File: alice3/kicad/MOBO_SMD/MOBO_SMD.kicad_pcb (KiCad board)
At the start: 2 copper layers, 90.4 x 49 mm, 53 parts, among them CON1 MicroSD, P1 CONN_01X05, P2 USB_OTG, P3 UART1, SW1 RESET, SW2 SOFT RESET, U1 VGA_daughter_board, U2 Propeller_P8X32A-D40, U3 24LC256, U4 Propeller_Plug, U5 STM32F415RG, U6 Z80CPU, U7 71V424S15PHGI8, U8 LD29080DT33R, Y1 5 MHz, Y2 16MHz, Y3 32.768KHz

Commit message: First pass at board layout.
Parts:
- removed C12, C13: 22pF, Capacitors_SMD:C_0805
- removed C18: 0.1 µF, Capacitors_SMD:C_0805
- removed R13, R5: 10k, Resistors_SMD:R_0805
- removed U7: 71V424S15PHGI8, TSOP44-II:TSOP44-II
- removed Y3: 32.768KHz, Crystals:Crystal_HC50-U_Vertical
- added C21: 1µ, Capacitors_SMD:C_0805, F.Cu at (180.5, 170.6)
- added C22: 4.7µ, Capacitors_SMD:C_1206, F.Cu at (171.0, 172.0)
- added F1: F_Small, Resistors_SMD:R_1210, F.Cu at (194.3, 83.8)
- added J1: VGA, Jac:00JG-DB15HDSOCKET, F.Cu at (165.1, 86.4)
- added R14: 240, Resistors_SMD:R_0805, F.Cu at (187.0, 134.0)
- added R15: 470, Resistors_SMD:R_0805, F.Cu at (187.0, 140.3)
- added R16: 240, Resistors_SMD:R_0805, F.Cu at (190.6, 134.0)
- added R17: 470, Resistors_SMD:R_0805, F.Cu at (204.5, 102.9)
- added R18: 240, Resistors_SMD:R_0805, F.Cu at (194.3, 134.0)
- added R19: 470, Resistors_SMD:R_0805, F.Cu at (190.6, 140.3)
- added R20: 240, Resistors_SMD:R_0805, F.Cu at (203.2, 127.0)
- added R21: 240, Resistors_SMD:R_0805, F.Cu at (194.3, 140.3)
- added R22: 10K, Resistors_SMD:R_0805, F.Cu at (176.7, 170.6)
- added R23: 10K, Resistors_SMD:R_0805, F.Cu at (201.9, 95.2)
- added R24: 100, Resistors_SMD:R_0805, F.Cu at (170.3, 178.5)
- added R25: 100, Resistors_SMD:R_0805, F.Cu at (176.7, 164.3)
- added REF**: 1pin, Connect:1pin, F.Cu at (113.0, 77.5)
- added REF**: 1pin, Connect:1pin, F.Cu at (113.0, 118.1)
- added REF**: 1pin, Connect:1pin, F.Cu at (195.6, 118.1)
- added REF**: 1pin, Connect:1pin, F.Cu at (195.6, 77.5)
- added X1: MINI_DIN_6, cui-md-xxs:cui-md-60s, F.Cu at (141.0, 74.9)
- C14, C19, C20: footprint Capacitors_ThroughHole:C_Radial_D5_L11_P2.5 -> Capacitors_SMD:C_1206
- D1: value DEBUG -> DEBUG LED; footprint LEDs:LED_0805 -> LEDs:LED-0805
- R1: value 100 -> 10k
- R11: value 1k -> 10k
- R12: value 1k -> 100
- SW1, SW2: footprint Buttons_Switches_ThroughHole:SW_PUSH_SMALL -> Buttons_Switches_SMD:SW_SPST_PTS645
- U1: value VGA_daughter_board -> Z80CPU-SMD; footprint Pin_Headers:Pin_Header_Straight_1x14 -> Housings_QFP:LQFP-44_10x10mm_Pitch0.8mm
- U2: value Propeller_P8X32A-D40 -> Propeller_P8X32A-Q44
- U6: value Z80CPU -> AS6C2008_TSOP; footprint Housings_QFP:LQFP-44_10x10mm_Pitch0.8mm -> SMD_Packages:TSOP32SP
- Y1: footprint Crystals:Crystal_HC50-U_Vertical -> Crystals:Crystal_HC49-SD_SMD
- Y2: footprint Crystals:Crystal_HC50-U_Vertical -> Crystals:ABM3
- moved Y2 58.8 mm to (113.0, 101.6), turned to 90 degrees
- moved C15 57.6 mm to (193.0, 92.7)
- moved U1 54.7 mm to (144.8, 101.6)
- moved C8 54.0 mm to (146.1, 132.1)
- moved Y1 53.7 mm to (224.8, 92.7)
- moved C11 51.5 mm to (138.4, 138.4)
- moved C4 44.4 mm to (131.3, 136.7)
- moved D1 41.1 mm to (141.0, 115.6), turned to 90 degrees
- moved U8 40.2 mm to (186.7, 86.4)
- moved D2 39.7 mm to (144.8, 115.6), turned to 90 degrees
- moved R2 38.8 mm to (213.4, 118.1)
- moved C3 37.5 mm to (152.7, 137.7)
- moved C5 37.5 mm to (152.9, 147.1)
- moved C6 37.5 mm to (144.0, 143.3)
- moved R10 37.5 mm to (148.1, 143.3)
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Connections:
- D1 pad 1: Net-(D1-Pad1) -> GND
- JP1 pad 1: Net-(JP1-Pad1) -> +3V3
- JP1 pad 2: GND -> Net-(JP1-Pad2)
- P2 pad 1: +5V -> Net-(F1-Pad1)
- P2 pad S4: (no net) -> GND
- R1 pad 1: Net-(D1-Pad1) -> Net-(R1-Pad1)
- R12 pad 1: +3V3 -> Net-(R1-Pad1)
- R12 pad 2: /BUSRQ -> Net-(D1-Pad2)
- R3 pad 1: +3V3 -> Net-(JP1-Pad2)
- R3 pad 2: Net-(JP1-Pad1) -> GND
- U1 pad 1: Net-(U1-Pad1) -> CLK
- U1 pad 10: Net-(U1-Pad10) -> D1
- U1 pad 11: KBD_DATA -> Net-(U1-Pad11)
- U1 pad 12: KBD_CLK -> +3V3
- U1 pad 13: +5V -> +3V3
- U1 pad 14: GND -> /HALT
- U1 pad 2: Net-(U1-Pad2) -> D4
- U1 pad 3: Net-(U1-Pad3) -> D3
- U1 pad 4: Net-(U1-Pad4) -> D5
- U1 pad 5: Net-(U1-Pad5) -> D6
- U1 pad 6: Net-(U1-Pad6) -> +3V3
- U1 pad 7: Net-(U1-Pad7) -> D2
- U1 pad 8: Net-(U1-Pad8) -> D7
- U1 pad 9: Net-(U1-Pad9) -> D0
- U2 pad 1: Net-(D1-Pad2) -> A7
- U2 pad 10: GND -> VGA_HSYNC
- U2 pad 11: /RESET -> VGA_B0
- U2 pad 12: +3V3 -> VGA_B1
- U2 pad 13: Net-(U1-Pad1) -> VGA_G0
- U2 pad 14: Net-(U1-Pad2) -> VGA_G1
- U2 pad 15: Net-(U1-Pad3) -> VGA_R1
- U2 pad 16: Net-(U1-Pad4) -> VGA_R0
- U2 pad 17: Net-(U1-Pad5) -> GND
- U2 pad 18: Net-(U1-Pad6) -> +3V3
- U2 pad 19: Net-(U1-Pad7) -> D0
- U2 pad 2: /IORQ -> CLK
- U2 pad 20: Net-(U1-Pad8) -> D1
- U2 pad 21: D0 -> D2
- U2 pad 22: D1 -> D3
- U2 pad 23: D2 -> D4
- U2 pad 24: D3 -> D5
- U2 pad 25: D4 -> D6
- U2 pad 26: D5 -> D7
- U2 pad 27: D6 -> GND
- U2 pad 28: D7 -> Net-(U2-Pad28)
- U2 pad 29: GND -> Net-(U2-Pad29)
- U2 pad 3: /WR -> Net-(P1-Pad5)
- U2 pad 30: Net-(U2-Pad30) -> +3V3
- U2 pad 31: Net-(U2-Pad31) -> A0
- U2 pad 32: +3V3 -> A1
- U2 pad 33: A0 -> A2
- U2 pad 34: A1 -> Net-(P1-Pad3)
- U2 pad 35: A2 -> Net-(U2-Pad35)
- U2 pad 36: Net-(P1-Pad3) -> Net-(R2-Pad2)
- U2 pad 38: Net-(R2-Pad2) -> Net-(U2-Pad38)
- U2 pad 39: Net-(U2-Pad39) -> GND
- U2 pad 4: /RD -> Net-(P1-Pad4)
- U2 pad 40: Net-(U2-Pad40) -> +3V3
- U2 pad 41: (no net) -> ~PROP_READY~
- U2 pad 42: (no net) -> /IORQ
- U2 pad 43: (no net) -> /WR
- U2 pad 44: (no net) -> /RD
- U2 pad 5: A7 -> GND
- U2 pad 6: CLK -> GND
- U2 pad 7: Net-(P1-Pad5) -> /RESET
- U2 pad 8: Net-(P1-Pad4) -> +3V3
- U2 pad 9: GND -> VGA_VSYNC
- U3 pad 6: Net-(U2-Pad37) -> Net-(U2-Pad35)
- U4 pad 3: Net-(U2-Pad40) -> Net-(U2-Pad38)
- U4 pad 4: Net-(U2-Pad39) -> Net-(U2-Pad37)
- U5 pad 28: GND -> Net-(R1-Pad1)
- U5 pad 3: Net-(C12-Pad1) -> ~PROP_READY~
- U5 pad 4: Net-(C13-Pad2) -> A17
- U5 pad 60: Net-(JP1-Pad1) -> Net-(JP1-Pad2)
- U6 pad 10: D6 -> A16
- U6 pad 11: +3V3 -> A14
- U6 pad 12: D2 -> A12
- U6 pad 13: D7 -> A7
- U6 pad 14: D0 -> A6
- U6 pad 15: D1 -> A5
- U6 pad 16: +3V3 -> A4
- U6 pad 17: +3V3 -> A3
- U6 pad 18: /HALT -> A2
- U6 pad 19: /MREQ -> A1
- U6 pad 2: A12 -> A9
- U6 pad 20: /IORQ -> A0
- U6 pad 21: /RD -> D0
- U6 pad 22: /WR -> D1
- U6 pad 23: /BUSACK -> D2
- U6 pad 24: +3V3 -> GND
- U6 pad 25: /BUSRQ -> D3
- U6 pad 26: /Z80_RESET -> D4
- U6 pad 27: Net-(U6-Pad27) -> D5
- U6 pad 28: Net-(U6-Pad28) -> D6
- U6 pad 29: GND -> D7
- U6 pad 3: A13 -> A8
- U6 pad 30: A0 -> /MREQ
- U6 pad 31: A1 -> A10
- U6 pad 32: A2 -> /RD
- U6 pad 4: A14 -> A13
- U6 pad 5: A15 -> /WR
- U6 pad 6: CLK -> GND
- U6 pad 7: D4 -> A15
- U6 pad 8: D3 -> +3V3
- U6 pad 9: D5 -> A17
- Y1 pad 1: Net-(U2-Pad30) -> Net-(U2-Pad28)
- Y1 pad 2: Net-(U2-Pad31) -> Net-(U2-Pad29)
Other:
- board size 90.4 x 49 mm -> 90.2 x 48.3 mm

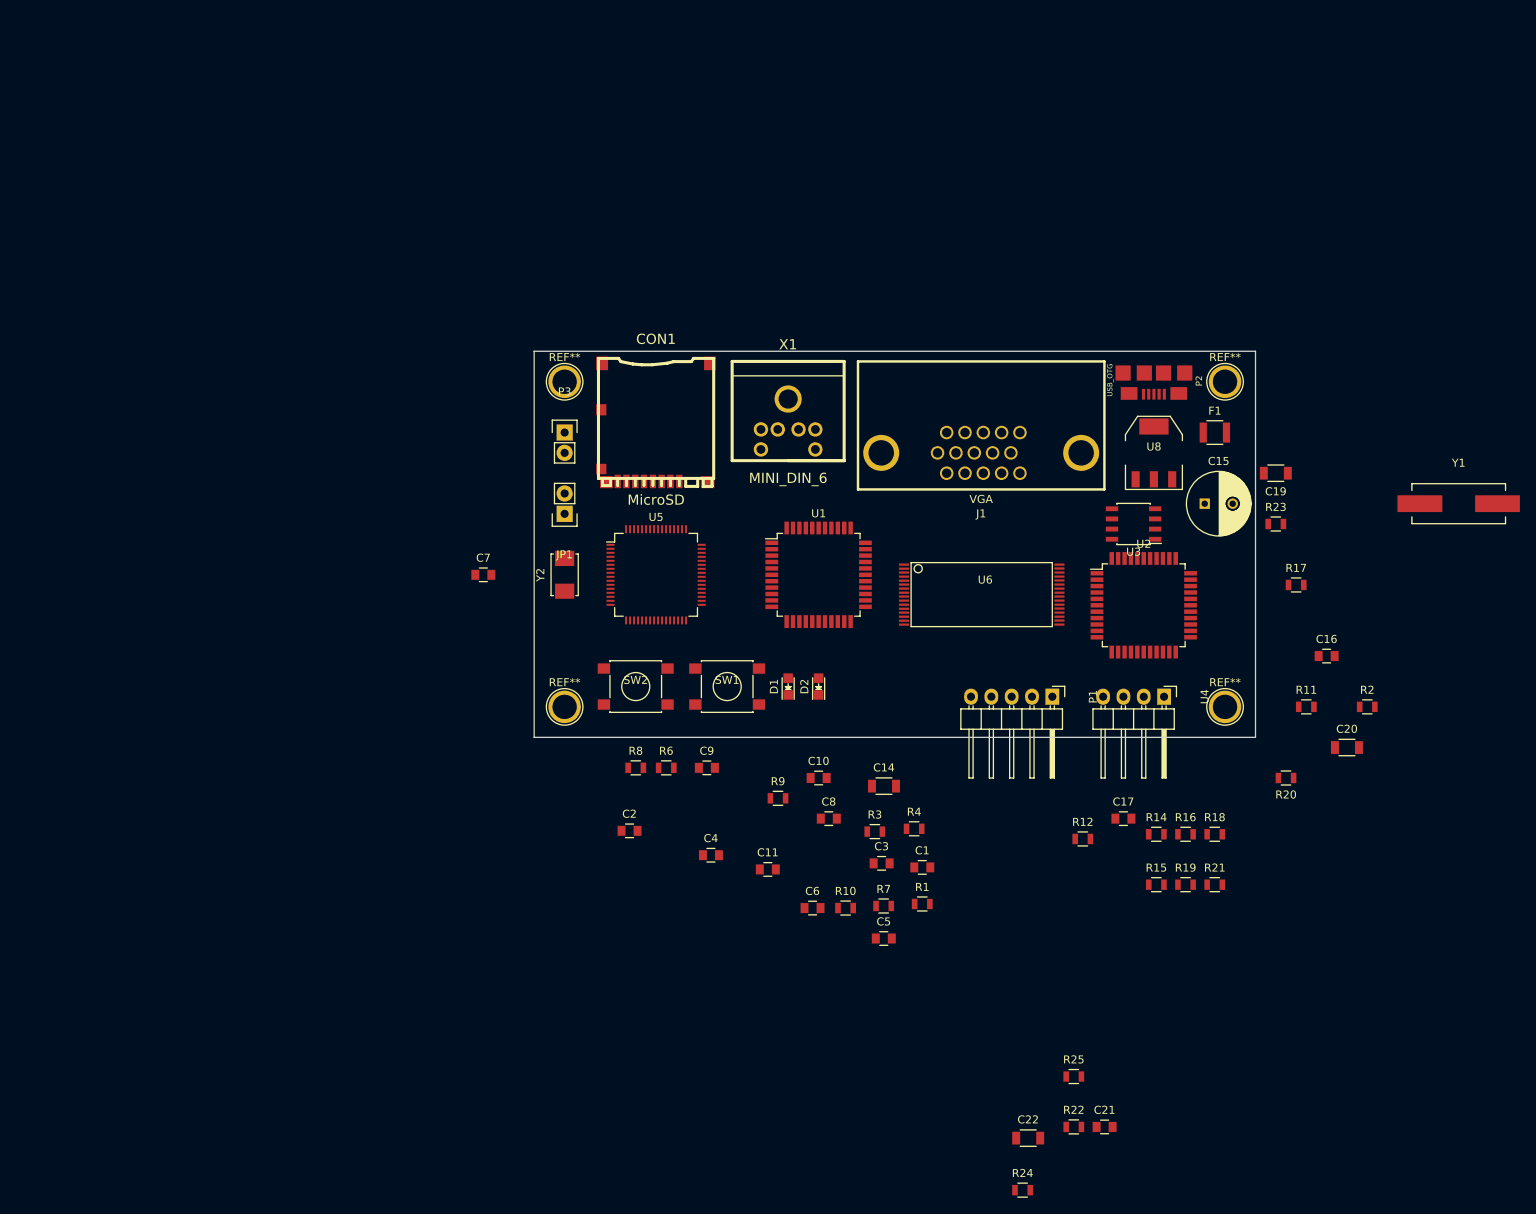
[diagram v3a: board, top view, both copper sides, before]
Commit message: Position all parts on PCB.
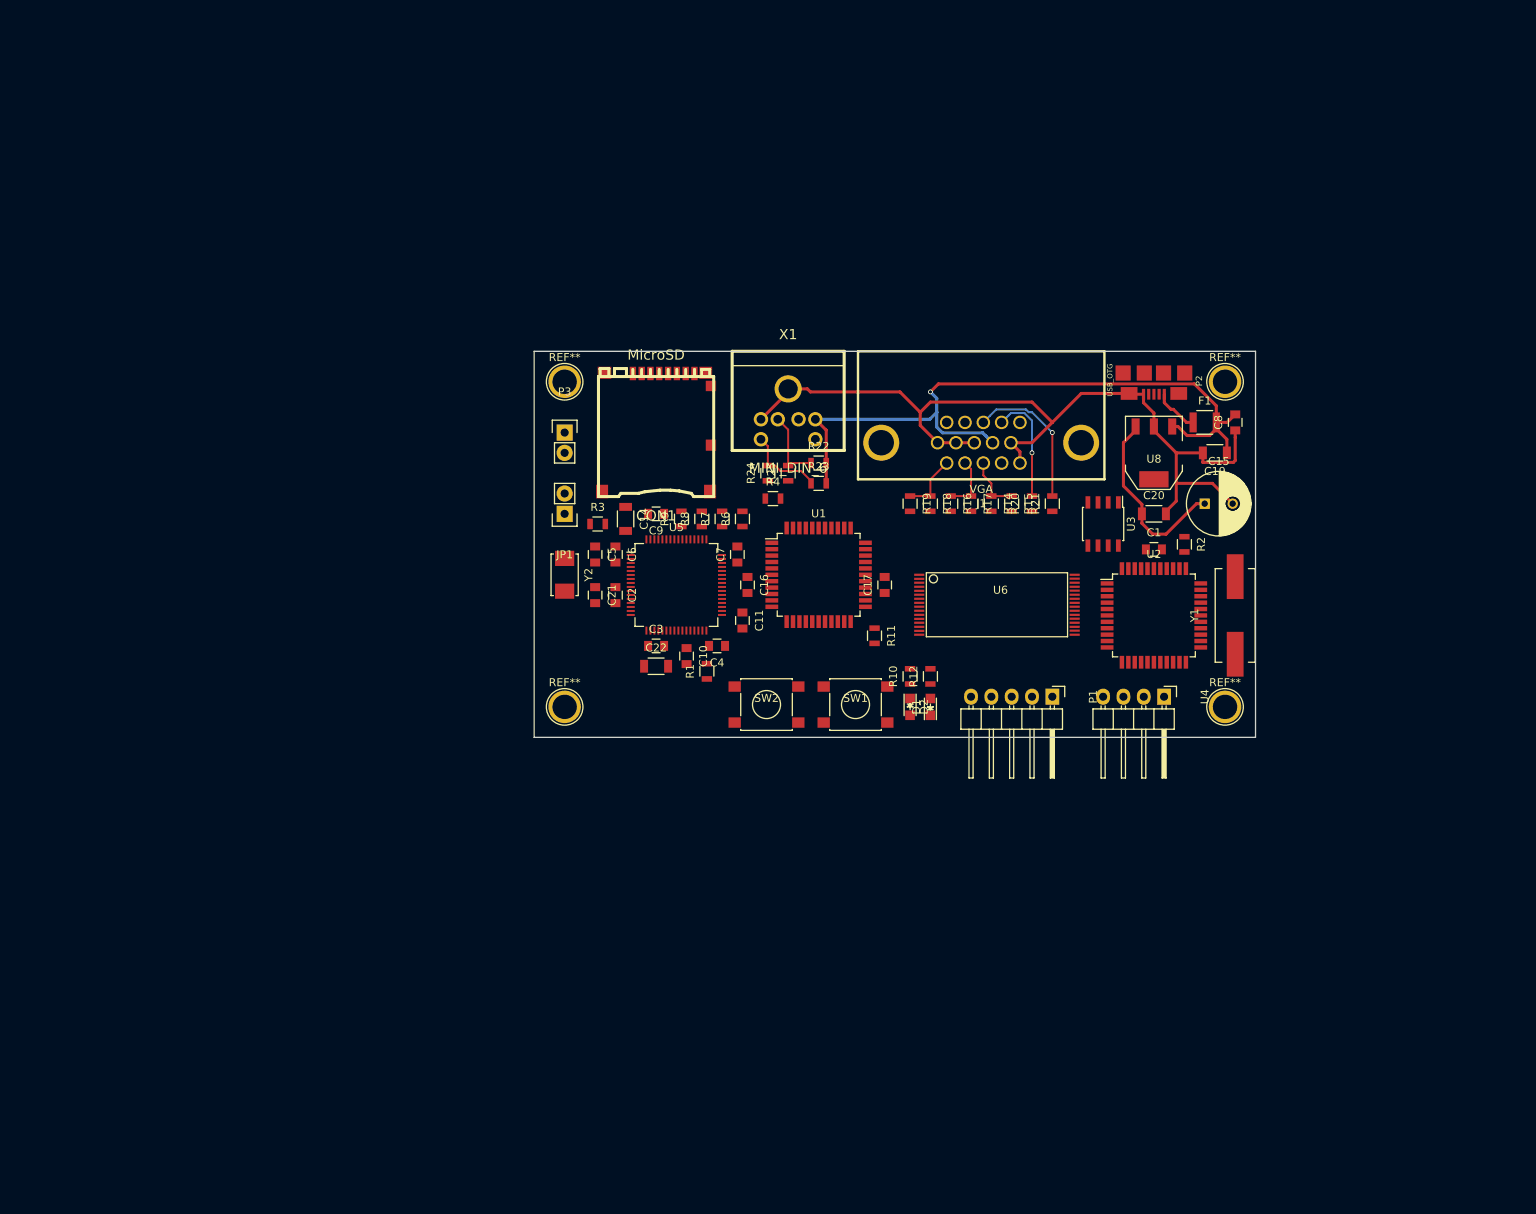
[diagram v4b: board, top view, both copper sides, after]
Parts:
- moved R24 95.1 mm to (138.4, 88.9), turned to 90 degrees
- moved C21 92.1 mm to (116.8, 104.1), turned to 270 degrees
- moved R22 88.9 mm to (144.8, 87.6)
- moved R25 83.4 mm to (141.0, 88.9), turned to 90 degrees
- moved C22 75.1 mm to (124.5, 113.0)
- moved C16 72.9 mm to (135.9, 102.9), turned to 270 degrees
- moved C8 70.9 mm to (196.8, 82.5), turned to 90 degrees
- moved C5 60.1 mm to (116.8, 99.1), turned to 270 degrees
- moved R19 58.8 mm to (156.2, 92.7), turned to 270 degrees
- moved R23 57.4 mm to (144.8, 90.2)
- moved R11 54.7 mm to (151.8, 109.2), turned to 270 degrees
- moved R18 54.5 mm to (158.8, 92.7), turned to 270 degrees
- moved R7 52.4 mm to (132.7, 94.6), turned to 90 degrees
- moved R21 51.8 mm to (174.0, 92.7), turned to 90 degrees
- moved R3 51.8 mm to (117.2, 95.2)
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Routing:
- net GND: track 0.00 -> 110.2 mm
- net +5V: track 0.00 -> 89.5 mm, vias 0 -> 1
- net +3V3: track 0.00 -> 23.7 mm
- net Net-(J1-Pad13): track 0.00 -> 18.4 mm, vias 0 -> 1
- net Net-(J1-Pad14): track 0.00 -> 14.1 mm, vias 0 -> 1
- net Net-(R23-Pad1): track 0.00 -> 10.1 mm
- net Net-(R22-Pad1): track 0.00 -> 9.32 mm
- net Net-(J1-Pad1): track 0.00 -> 7.51 mm
- net Net-(J1-Pad3): track 0.00 -> 7.09 mm
- net Net-(J1-Pad2): track 0.00 -> 6.98 mm
- net Net-(F1-Pad1): track 0.00 -> 5.68 mm
- net (no net): track 0.00 -> 0.51 mm
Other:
- net class Power added: clearance 0.2, trace_width 0.381, via_dia 0.6, via_drill 0.4

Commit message: Route about 50 traces.
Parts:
- moved P1 2.54 mm to (174.0, 119.4)
- moved U4 2.54 mm to (188.0, 119.4)
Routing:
- net +3V3: track 23.7 -> 175.3 mm, vias 0 -> 2
- net GND: track 110.2 -> 244.2 mm, vias 0 -> 17
- net A15: track 0.00 -> 52.8 mm, vias 0 -> 2
- net A12: track 0.00 -> 52.7 mm, vias 0 -> 4
- net A14: track 0.00 -> 49.8 mm, vias 0 -> 4
- net A13: track 0.00 -> 46.4 mm, vias 0 -> 2
- net VGA_R0: track 0.00 -> 42.4 mm, vias 0 -> 2
- net D7: track 0.00 -> 41.8 mm
- net A11: track 0.00 -> 39.0 mm, vias 0 -> 2
- net VGA_R1: track 0.00 -> 38.7 mm, vias 0 -> 2
- net D6: track 0.00 -> 38.6 mm
- net D5: track 0.00 -> 35.3 mm
- net VGA_G1: track 0.00 -> 35.2 mm, vias 0 -> 2
- net VGA_G0: track 0.00 -> 32.5 mm, vias 0 -> 2
- net D4: track 0.00 -> 30.9 mm
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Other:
- net class Power: trace_width 0.381 -> 0.2794
